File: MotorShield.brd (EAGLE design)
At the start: 85 x 56 mm, 119 parts, among them IC1 OPA4340E, IC2 OPA4340E, IC3 74HCT125D, X1 MSTBV2, X2 MSTBV8, X3 MSTBV8, X4 INPUTS, X5 BUTTON_LED, X6 DOTSTARS

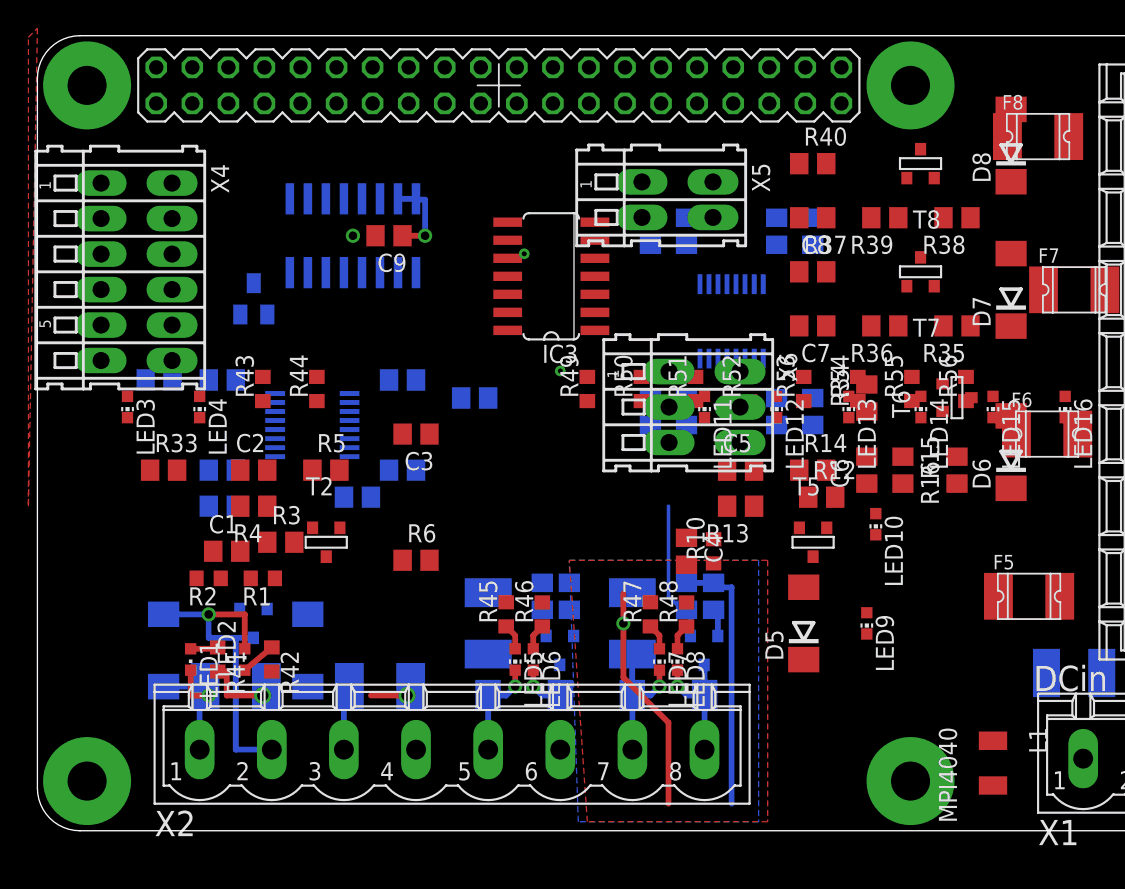
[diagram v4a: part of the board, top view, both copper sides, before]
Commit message: routed M1 to M4
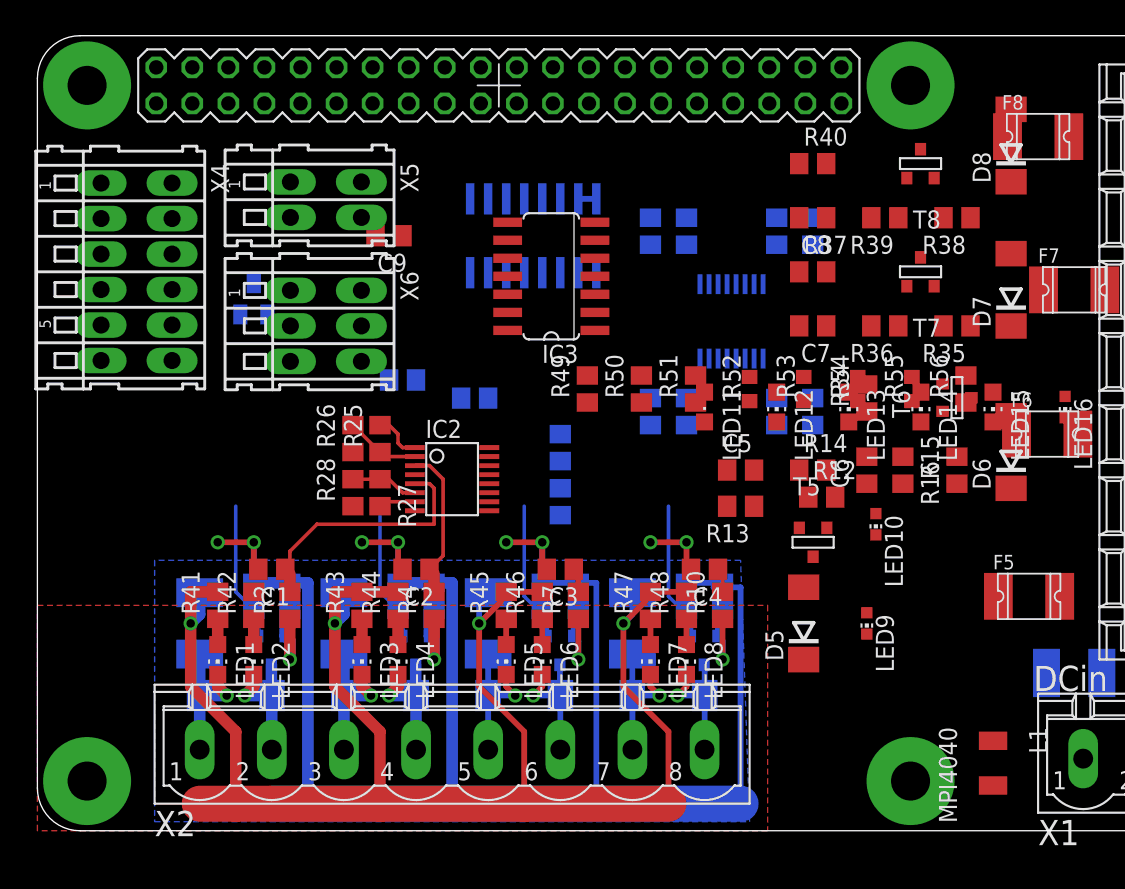
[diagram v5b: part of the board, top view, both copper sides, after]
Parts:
- F1, F2, F3, F4, F5, F6, F7, F8: value 1812L -> 1A
- LED1, LED2: device led:CHIPLED_0603 -> led:CHIP-LED0805
- LED11: device led:CHIP-LED0603 -> led:CHIPLED_0805
- LED12, LED13, LED14, LED15, LED3, LED4, LED5, LED6, LED7, LED8: device led:CHIP-LED0603 -> led:CHIP-LED0805
- R1, R10, R2, R41, R42, R43, R44, R45, R46, R47, R48, R49, R50, R51, R56: device rcl:R0603 -> rcl:R0805
- moved X6 27.3 mm to (20.3, 35.6)
- moved X5 24.8 mm to (20.3, 44.5)
- moved LED3 24.3 mm to (22.9, 12.1)
- moved LED4 22.6 mm to (25.4, 12.1)
- moved R43 16.8 mm to (22.9, 15.9)
- moved R44 16.3 mm to (25.4, 15.9)
- moved R28 15.8 mm to (22.2, 23.8), flipped to the top, turned to 90 degrees
- moved R32 14.7 mm to (36.8, 27.0), turned to 270 degrees
- moved R4 14.5 mm to (27.9, 15.9), turned to 90 degrees
- moved C3 13.9 mm to (36.8, 18.4)
- moved R27 13.7 mm to (24.1, 23.8), flipped to the top, turned to 270 degrees
- moved C2 13.4 mm to (26.7, 18.4), turned to 180 degrees
- moved U$1 12.7 mm to (34.9, 41.9)
- moved R6 11.7 mm to (38.1, 16.5), flipped to the bottom, turned to 270 degrees
- moved R3 11.4 mm to (27.9, 16.5), flipped to the bottom, turned to 270 degrees
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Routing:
- net GND: track 18.7 -> 137.9 mm, vias 1 -> 8
- net +24V: track 26.0 -> 120.5 mm, vias 3 -> 4
- net V7: track 0.00 -> 18.3 mm
- net N$2: track 23.4 -> 9.66 mm
- net V6: track 0.00 -> 10.8 mm
- net M5: track 0.00 -> 9.97 mm
- net M6: track 0.00 -> 9.79 mm
- net M7: track 0.00 -> 9.79 mm
- net N$10: track 0.00 -> 9.66 mm, vias 0 -> 1
- net N$18: track 0.00 -> 6.64 mm, vias 0 -> 1
- net N$3: track 0.00 -> 6.64 mm, vias 0 -> 1
- net N$11: track 0.00 -> 6.64 mm, vias 0 -> 1
- net N$17: track 3.33 -> 9.66 mm
- net N$13: track 4.82 -> 10.4 mm, vias 0 -> 1
- net N$31: track 0.00 -> 5.28 mm
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- removed copper zone on layer 1, net GND

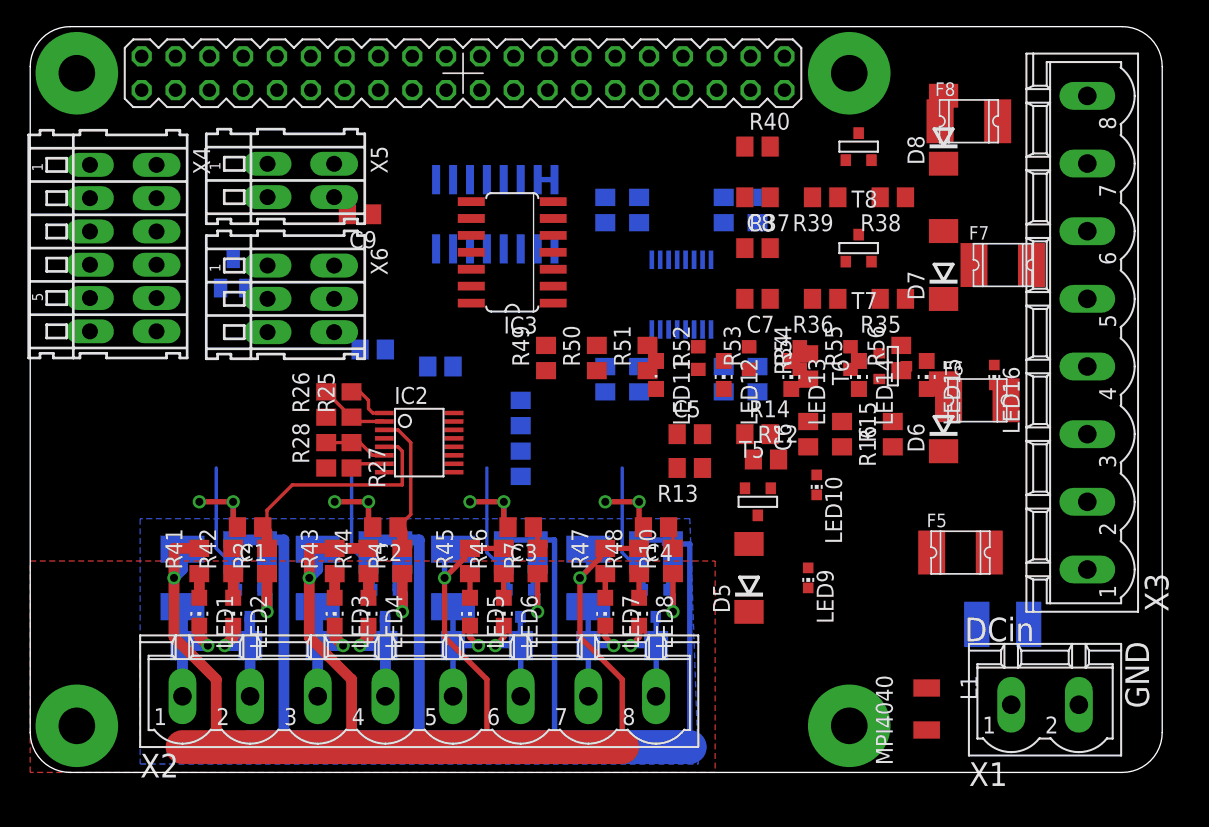
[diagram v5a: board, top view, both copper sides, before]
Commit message: placed parts for M5-M6
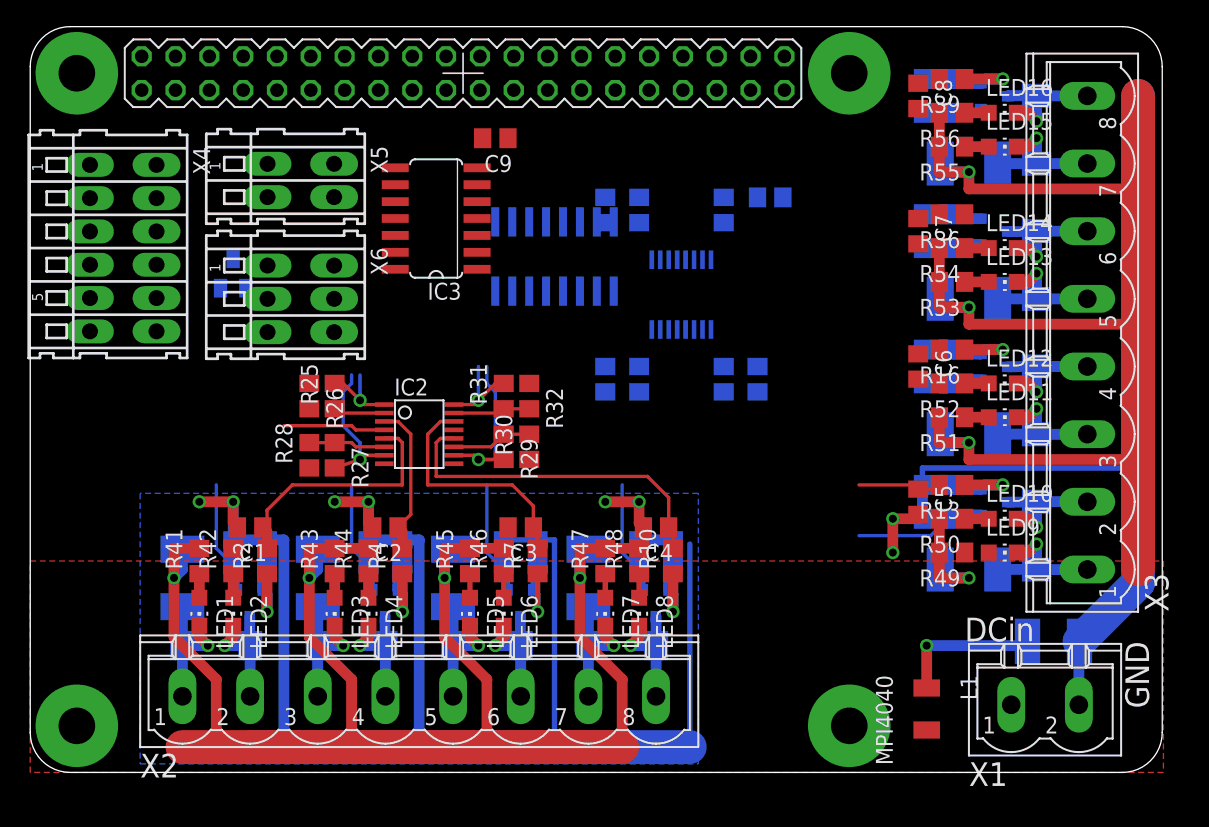
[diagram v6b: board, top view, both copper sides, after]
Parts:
- LED10, LED16, LED9: device led:CHIP-LED0603 -> led:CHIP-LED0805
- LED11: device led:CHIPLED_0805 -> led:CHIP-LED0805
- R52, R53, R54, R55: device rcl:R0603 -> rcl:R0805
- moved R49 33.8 mm to (69.2, 16.5), turned to 180 degrees
- moved R50 29.3 mm to (69.2, 19.1), turned to 180 degrees
- moved LED11 26.2 mm to (73.0, 26.7), turned to 270 degrees
- moved R51 23.3 mm to (69.2, 26.7), turned to 180 degrees
- moved D5 21.8 mm to (75.6, 17.8), flipped to the bottom
- moved LED12 21.0 mm to (73.0, 29.2), turned to 270 degrees
- moved R13 19.7 mm to (69.2, 21.6)
- moved LED16 19.7 mm to (73.0, 49.5), turned to 270 degrees
- moved R52 19.1 mm to (69.2, 29.2), turned to 180 degrees
- moved R56 18.8 mm to (69.2, 49.5), turned to 180 degrees
- moved LED15 18.1 mm to (73.0, 47.0), turned to 270 degrees
- moved C5 17.9 mm to (66.7, 20.3), turned to 270 degrees
- moved T5 17.8 mm to (72.4, 20.3), flipped to the bottom, turned to 270 degrees
- moved R55 17.6 mm to (69.2, 47.0), turned to 180 degrees
- moved LED13 17.3 mm to (73.0, 36.8), turned to 270 degrees
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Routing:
- net +24V: track 120.5 -> 246.9 mm, vias 4 -> 9
- net GND: track 137.9 -> 200.9 mm
- net V4: track 1.72 -> 26.1 mm
- net V5: track 1.72 -> 18.1 mm
- net CH4: track 0.00 -> 13.0 mm, vias 0 -> 1
- net N$5: track 0.00 -> 10.4 mm, vias 0 -> 1
- net N$8: track 0.00 -> 10.4 mm, vias 0 -> 1
- net N$7: track 0.00 -> 10.4 mm, vias 0 -> 1
- net N$4: track 0.00 -> 10.4 mm, vias 0 -> 1
- net M3: track 0.00 -> 10.2 mm
- net N$57: track 0.00 -> 9.66 mm, vias 0 -> 1
- net N$38: track 0.00 -> 9.66 mm, vias 0 -> 1
- net N$51: track 0.00 -> 9.66 mm, vias 0 -> 1
- net N$45: track 0.00 -> 9.64 mm, vias 0 -> 1
- net CH7: track 2.59 -> 11.1 mm, vias 0 -> 1
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
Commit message: routed op-amps
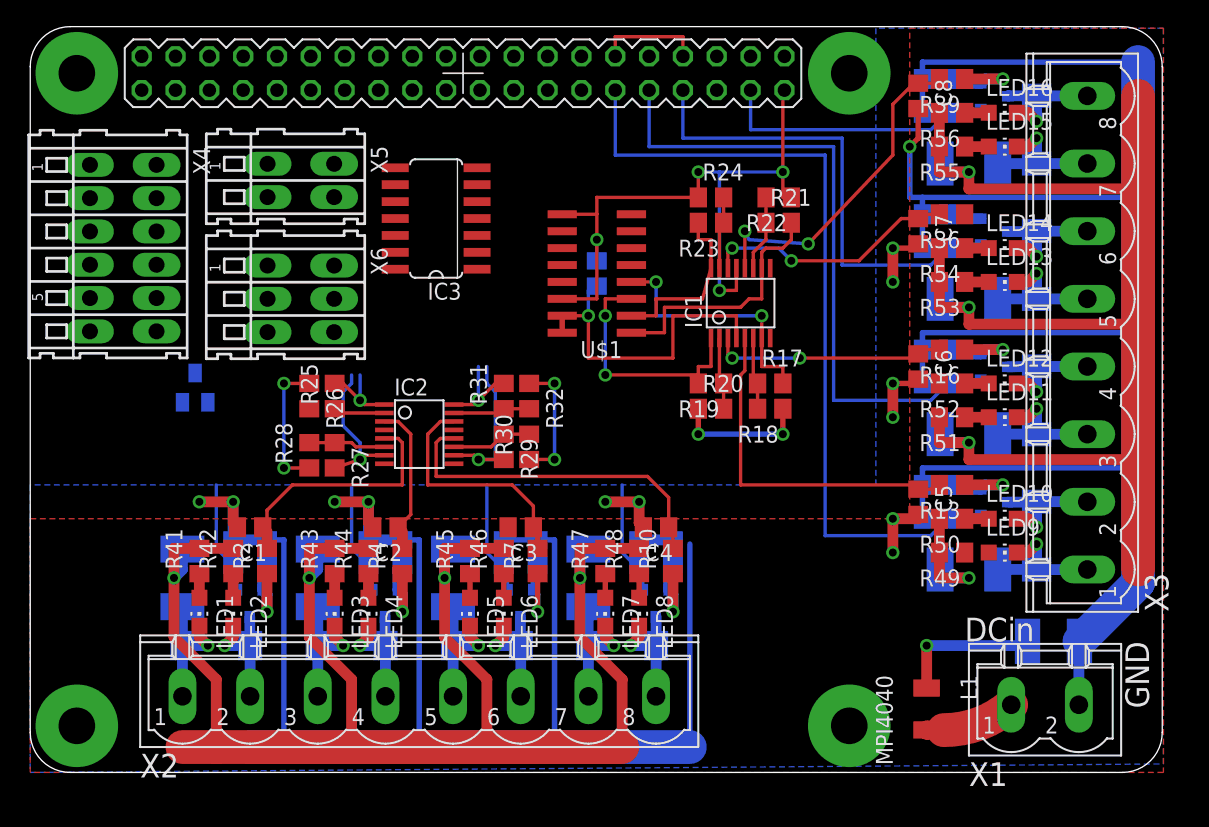
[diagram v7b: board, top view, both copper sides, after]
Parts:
- C10: value (none) -> 22uF
- T1, T2, T3, T4, T5, T6, T7, T8: value (none) -> FDN337N
- T9: value (none) -> BC847C
- moved R22 13.1 mm to (56.2, 43.2), flipped to the top, turned to 180 degrees
- moved C9 12.7 mm to (42.5, 37.5), flipped to the bottom, turned to 90 degrees
- moved R18 12.6 mm to (55.6, 27.3), flipped to the top, turned to 180 degrees
- moved R21 10.5 mm to (56.2, 41.3), flipped to the top, turned to 0 degrees
- moved R17 9.85 mm to (55.6, 29.2), flipped to the top, turned to 0 degrees
- moved T9 9.04 mm to (12.4, 28.9)
- moved IC1 4.49 mm to (53.3, 35.2), flipped to the top
- moved R24 4.45 mm to (51.1, 43.2), flipped to the top, turned to 0 degrees
- moved R20 4.14 mm to (51.1, 27.3), flipped to the top, turned to 0 degrees
- moved U$1 3.42 mm to (42.5, 37.5), flipped to the top, turned to 90 degrees
- moved R23 1.35 mm to (51.1, 41.3), flipped to the top, turned to 180 degrees
- moved R19 1.00 mm to (51.1, 29.2), flipped to the top, turned to 180 degrees
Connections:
- removed net +3,3V: IC1.4, IC2.4, PCB1.17
- net +3V3: now also IC1.4, IC2.4, PCB1.17
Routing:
- net GND: track 200.9 -> 369.5 mm, vias 8 -> 23
- net M3: track 10.2 -> 61.9 mm
- net M2: track 2.59 -> 49.2 mm
- net M1: track 2.59 -> 36.1 mm
- net V0: track 0.00 -> 25.4 mm, vias 0 -> 2
- net +3V3: track 1.27 -> 25.0 mm, vias 0 -> 1
- net M0: track 0.00 -> 20.9 mm
- net V3: track 6.68 -> 26.7 mm
- net CH2: track 0.00 -> 19.7 mm, vias 0 -> 2
- net CH0: track 0.00 -> 19.3 mm
- net V1: track 0.00 -> 19.0 mm, vias 0 -> 2
- net CH3: track 0.00 -> 19.0 mm, vias 0 -> 2
- net V2: track 0.00 -> 17.6 mm, vias 0 -> 2
- net CH1: track 0.00 -> 13.4 mm
- net +3,3V: track 7.67 -> 0.00 mm
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
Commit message: more routing
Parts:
- moved IC3 0.95 mm to (30.5, 40.6)
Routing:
- net GND: track 369.5 -> 421.5 mm, vias 23 -> 24
- net M6: track 8.52 -> 54.1 mm
- net CH7: track 11.1 -> 49.1 mm, vias 1 -> 2
- net CH6: track 6.29 -> 43.7 mm, vias 1 -> 2
- net M7: track 8.52 -> 40.2 mm
- net CH5: track 6.93 -> 36.1 mm, vias 1 -> 2
- net CH4: track 13.0 -> 40.3 mm, vias 1 -> 2
- net +3V3: track 25.0 -> 51.3 mm, vias 1 -> 2
- net DOUT: track 0.00 -> 1.84 mm
